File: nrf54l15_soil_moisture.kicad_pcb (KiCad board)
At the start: 4 copper layers, 76.4 x 51 mm, 60 parts, among them CN1 SM04B-SRSS-TB, J2 TC2030, J3 USB_C_Receptacle_PowerOnly_6P, U1 nRF54L15-QDXX, U2 nPM1300-QEXX, U3 SPV1040T, U4 S2B-PH-K-S-GW, X1 XL7EL89CKI-111YLC-32M

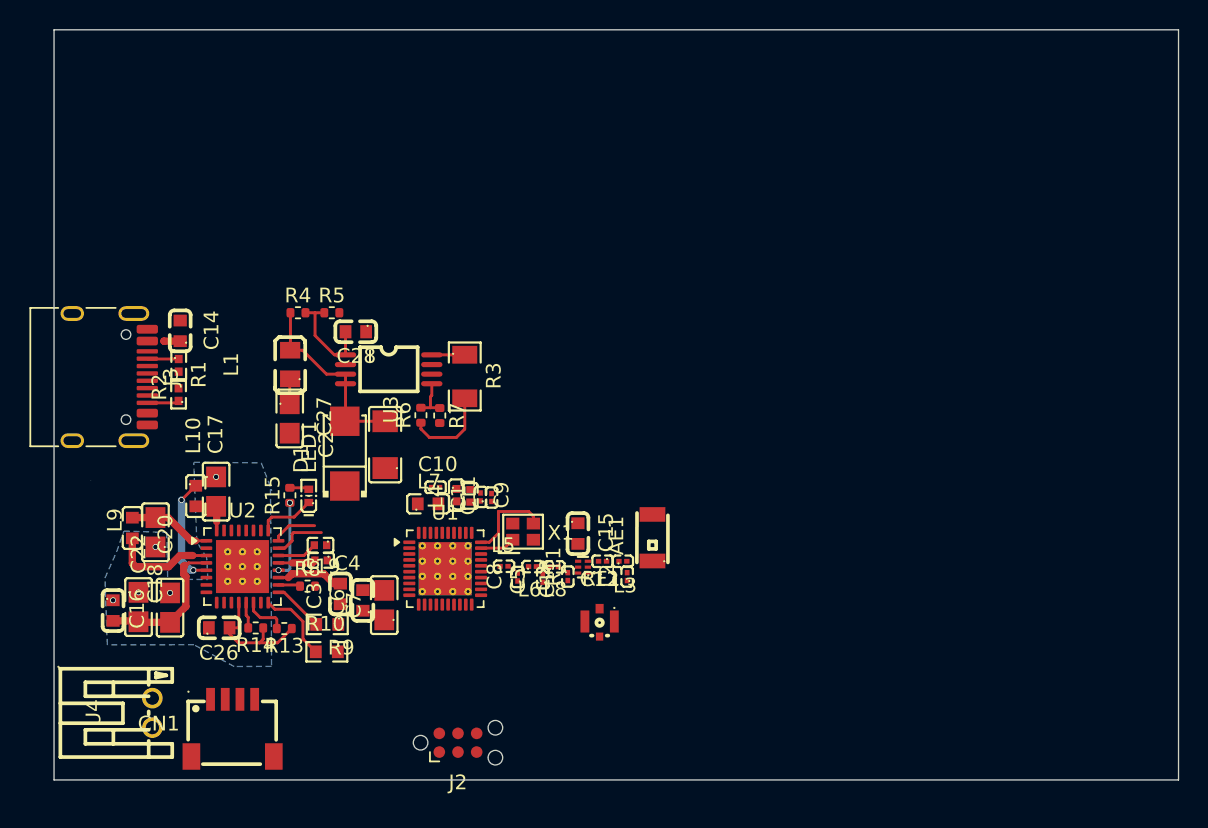
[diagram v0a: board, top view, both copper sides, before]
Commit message: Update soil moisture PCB layout and npm1300 VDDIO routing.
Co-authored-by: Cursor <cursoragent@cursor.com>
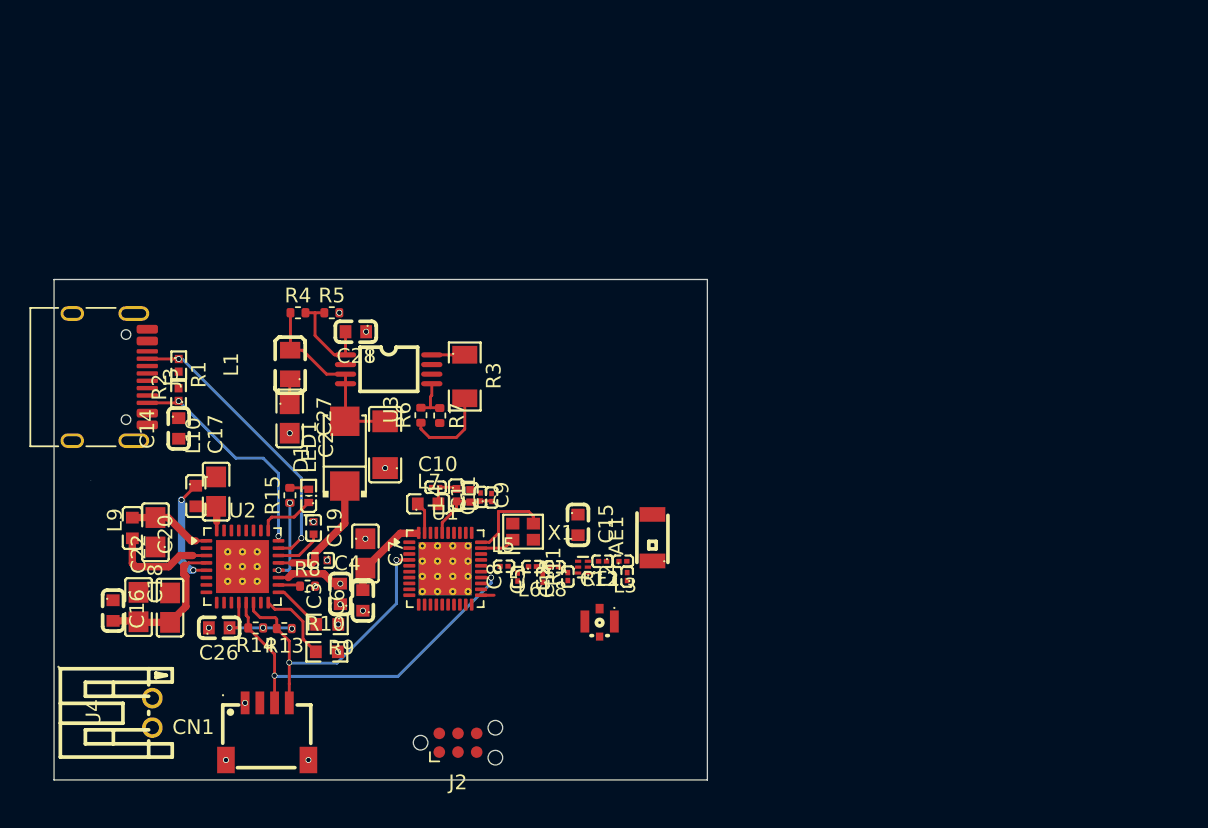
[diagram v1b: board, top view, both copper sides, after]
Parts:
- moved C14 6.63 mm to (102.2, 78.2), turned to -90 degrees
- moved C7 3.74 mm to (114.9, 86.7), turned to -90 degrees
- moved CN1 2.36 mm to (108.2, 98.8)
- moved C19 1.26 mm to (111.4, 84.9), turned to -90 degrees
- moved C15 0.59 mm to (129.3, 84.7)
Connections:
- C16 pad 1: VSYS_GND -> GND
- C17 pad 1: VSYS_GND -> GND
- C18 pad 1: VSYS_GND -> GND
- C20 pad 1: (no net) -> GND
- C22 pad 1: VSYS_GND -> GND
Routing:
- net I2C_SDA: track 1.78 -> 26.0 mm, vias 0 -> 2
- net I2C_SCL: track 3.01 -> 21.2 mm, vias 0 -> 2
- net CC1: track 5.76 -> 19.7 mm, vias 0 -> 2
- net CC2: track 5.24 -> 15.6 mm, vias 0 -> 2
- net VOUT1: track 5.69 -> 11.7 mm
- net Net-(U1-DECA): track 0.00 -> 4.99 mm
- net VBUS: track 3.65 -> 8.43 mm
- net Net-(U1-DECD): track 0.00 -> 2.36 mm
- net Net-(U1-DCC): track 0.00 -> 2.16 mm
- net VDDIO: track 8.74 -> 6.59 mm, vias 0 -> 3
- net ANT_SEL: track 0.00 -> 0.89 mm
- net VBUSOUT: track 2.72 -> 3.24 mm
- net VSYS_GND: track 0.08 -> 0.00 mm, vias 5 -> 0
- net VBAT: vias 0 -> 1
- net GND: vias 0 -> 16
- added copper zone on In2.Cu, net VBAT
- removed copper zone on B.Cu, net VSYS_GND
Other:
- board size 76.4 x 51 mm -> 44.4 x 34 mm
